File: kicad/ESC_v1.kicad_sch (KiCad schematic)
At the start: 21 parts, among them Q1 CSD17573Q5B, Q2 CSD17573Q5B, Q3 CSD17573Q5B, Q4 CSD17573Q5B, Q5 CSD17573Q5B, Q6 CSD17573Q5B, U1 STM32H503CBUx, U2 LM5106MMX, U3 LM5106MMX, U4 LM5106MMX

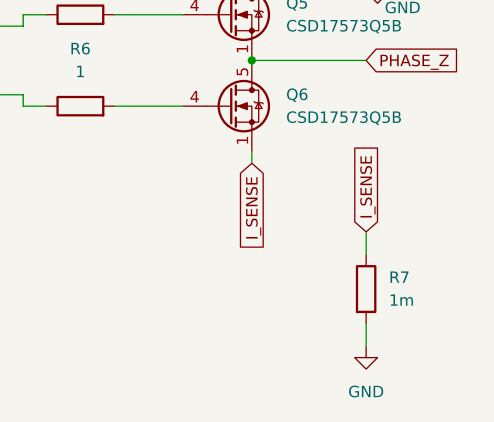
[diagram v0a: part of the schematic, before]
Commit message: fixed parts library
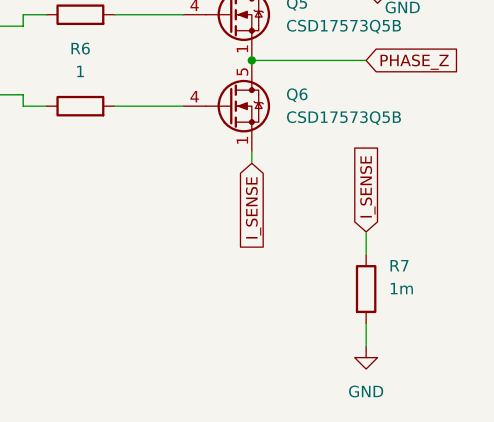
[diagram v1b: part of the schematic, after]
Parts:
- removed R7: 1m, Resistor_SMD:R_2512_6332Metric, symbol Device:R
- added R7: ${Resistance}, Resistor_SMD:R_2512_6332Metric, symbol libdb:Resistors/RES-1
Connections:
- net GND: now also R7.2
- net I_SENSE: now also R7.1
